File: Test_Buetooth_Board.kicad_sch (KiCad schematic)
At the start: 7 parts, among them U1 WH-BLE103a, U2 YM23, U3 HLK-B40, U4 WL6601-TC, U5 E104-BT52, U6 E104-BT01, U7 E104-BT5010A

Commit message: SCH: Se termina la primera versión del sch. PCB: Se ordenan unos componentes
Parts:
- added C1, C11, C13, C15, C16, C18, C19, C2, C21, C4, C5, C7, C9: 100n, 1-Capacitor:C_0805_2012Metric, symbol Device:C_Small
- added C10, C12, C14, C17, C20, C3, C8: 10n, 1-Capacitor:C_0805_2012Metric, symbol Device:C_Small
- added D1, D2, D3, D4, D5, D6, D7: LED, 1-Led:LED_0805, symbol Device:LED
- added J1: Screw_Terminal_01x04, Connector_PinHeader_2.54mm:PinHeader_1x04_P2.54mm_Vertical, symbol Connector:Screw_Terminal_01x04
- added J12, J13, J14, J15, J17, J18, J19, J20, J21, J22, J24, J25, J26, J29, J30, J31, J4, J5, J6, J7, J8, J9: Screw_Terminal_01x02, Connector_PinHeader_2.54mm:PinHeader_1x02_P2.54mm_Vertical, symbol Connector:Screw_Terminal_01x02
- added J16, J23, J27: Screw_Terminal_01x05, Connector_PinHeader_2.54mm:PinHeader_1x05_P2.54mm_Vertical, symbol Connector:Screw_Terminal_01x05
- added J28, J33: Screw_Terminal_01x06, Connector_PinHeader_2.54mm:PinHeader_1x06_P2.54mm_Vertical, symbol Connector:Screw_Terminal_01x06
- added J32: Screw_Terminal_01x07, 1-Pinhead:PinHeader_1x07_P2.54mm_Vertical, symbol Connector:Screw_Terminal_01x07
- added J34: Screw_Terminal_01x08, Connector_PinHeader_2.54mm:PinHeader_1x08_P2.54mm_Vertical, symbol Connector:Screw_Terminal_01x08
- added Q1, Q2, Q3, Q4, Q5, Q6, Q7: MMBT3904, Package_TO_SOT_SMD:SOT-23, symbol Transistor_BJT:MMBT3904
- added R1, R18, R2, R37, R41, R7: 100, 1-Resistor:R_0805_2012Metric, symbol Device:R_Small
- added R10, R13, R16, R17, R19, R21, R24, R26, R27, R29, R31, R32, R33, R35, R38, R39, R40, R42, R43, R5: 10k, 1-Resistor:R_0805_2012Metric, symbol Device:R_Small
- added R11, R15, R22, R25, R30, R36, R4: 2k2, 1-Resistor:R_0805_2012Metric, symbol Device:R_Small
- added R12, R20, R23, R28, R3, R34, R6, R9: 1k, 1-Resistor:R_0805_2012Metric, symbol Device:R_Small
- added R8: 10K, 1-Resistor:R_0805_2012Metric, symbol Device:R_Small
- added S1, S2, S3, S5, S6, S7, S8: 10-XX, 1-Switch:SW_PUSH_6mm_H7.3mm, symbol 1-Switch:10-XX
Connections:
- net GND: now reaches U3.1 (GND)
- net GND: now also U1.13 (GND), U1.15 (GND), U2.24 (GND), U3.10 (GND), U3.28 (GND), U4.2 (GND), U5.1 (GND), U5.12 (GND), U5.18 (GND), U5.5 (GND), U5.6 (GND), U6.1 (GND), U7.1 (GND), U7.16 (GND), U7.9 (GND), C1.2, C10.2, C11.2, C12.2, C13.2, C14.2, C15.2, C16.2, C17.2, C18.2, C19.2, C2.2, C20.2, C21.2, C3.2, C4.2, C5.2, C7.2, C8.2, C9.2, D3.1 (K), D4.1 (K), D5.1 (K), D7.1 (K), J1.4 (Pin_4), Q1.2 (E), Q2.2 (E), Q3.2 (E), Q4.2 (E), Q5.2 (E), Q6.2 (E), Q7.2 (E), R1.2, R10.2, R13.2, R16.2, R17.2, R18.2, R19.2, R2.2, R21.2, R24.2, R27.2, R29.2, R31.2, R32.2, R35.2, R37.2, R39.2, R40.2, R41.2, R5.2, R7.2
- net PC7_SLEEP_OUTPUT: now reaches U3.16 (PC7)
- net PC7_SLEEP_OUTPUT: now also J16.1 (Pin_1), R20.2
- net PC6_SLEEP_INPUT: now reaches U3.17 (PC6)
- net PC6_SLEEP_INPUT: now also J16.2 (Pin_2), R17.1
- net PC5_KEY_INPUT: now reaches U3.18 (PC5)
- net PC5_KEY_INPUT: now also J16.3 (Pin_3), R19.1
- net TX3: now reaches U3.23 (TXD)
- net TX3: now also J13.2 (Pin_2)
- net RX3: now reaches U3.24 (RXD)
- net RX3: now also J14.2 (Pin_2)
- net PA4_CONNECTED_OUTPUT: now reaches U3.25 (PA4)
- net PA4_CONNECTED_OUTPUT: now also J16.4 (Pin_4), R23.2
- net PA4_MODE_OUTPUT: now reaches U3.26 (PA5)
- net PA4_MODE_OUTPUT: now also J16.5 (Pin_5)
- net RST_3: now reaches U3.7 (RESET)
- net RST_3: now also R16.1, S5.3 (P)
- net VCC3: now reaches U3.9 (VBAT)
- net VCC3: now also C10.1, C9.1, J12.2 (Pin_2), R22.1, R25.1, S5.1 (S)
- net VCC7: now reaches U7.17 (VCC)
- net VCC7: now also C19.1, C20.1, J29.2 (Pin_2)
- net RX7: now reaches U7.18 (RXD)
- net RX7: now also J31.2 (Pin_2)
- net TX7: now reaches U7.19 (TXD)
- net TX7: now also J30.2 (Pin_2)
- net RTS_7: now reaches U7.20 (RTS)
- net RTS_7: now also J32.6 (Pin_6)
- net CTS_7: now reaches U7.21 (CTS)
- net CTS_7: now also J32.7 (Pin_7)
- net RST_7: now reaches U7.22 (RST)
- net RST_7: now also C21.1, R43.2, S8.1 (S)
- net MOD_7: now reaches U7.4 (MOD)
- net MOD_7: now also J32.1 (Pin_1), R39.1
- net WKP_7: now reaches U7.5 (WKP)
- net WKP_7: now also J32.2 (Pin_2), R40.1
- net DISC_7: now reaches U7.6 (DISC)
- net DISC_7: now also J32.3 (Pin_3), R42.2
- net LINK_7: now reaches U7.7 (LINK)
- net LINK_7: now also J32.4 (Pin_4)
- net DATA_7: now reaches U7.8 (DATA)
- net DATA_7: now also J32.5 (Pin_5)
- net SWCLK_5: now reaches U5.10 (CLK)
- net SWCLK_5: now also J23.2 (Pin_2)
- net WKP_5: now reaches U5.13 (WKP)
- net WKP_5: now also J23.3 (Pin_3), R27.1
- net TX5: now reaches U5.14 (TXD)
- net TX5: now also J20.2 (Pin_2)
- net RX5: now reaches U5.15 (RXD)
- net RX5: now also J21.2 (Pin_2)
- net LINK_5: now reaches U5.16 (LINK)
- net LINK_5: now also J23.4 (Pin_4), R28.2
- net DATA_5: now reaches U5.17 (DATA)
- net DATA_5: now also J23.5 (Pin_5)
- net VCC5: now reaches U5.3 (VCC)
- net VCC5: now also U5.4 (VH+), C13.1, C14.1, D6.2 (A), J22.2 (Pin_2), R26.1, R38.1, R43.1
- net RST_5: now reaches U5.7 (RST)
- net RST_5: now also C15.1, R26.2, S6.1 (S)
- net SWDIO_5: now reaches U5.8 (SWDIO)
- net SWDIO_5: now also J23.1 (Pin_1)
- net LINK_6: now reaches U6.10 (P1.5_LINK)
- net LINK_6: now also J27.4 (Pin_4), R34.2
- net DATA_6: now reaches U6.11 (P1.4_DATA)
- net DATA_6: now also J27.5 (Pin_5)
- net WKP_6: now reaches U6.13 (P1.2_WKP)
- net WKP_6: now also J28.1 (Pin_1), R32.1
- net P0.7: now reaches U6.16 (P0.7_AT)
- net P0.7: now also J28.2 (Pin_2)
- net P0.6: now reaches U6.17 (P0.6_AT)
- net P0.6: now also J28.3 (Pin_3)
- net DISC_6: now reaches U6.18 (P0.5_DISC)
- net DISC_6: now also J28.4 (Pin_4), R33.1
- net VCC6: now reaches U6.2 (VCC)
- net VCC6: now also C16.1, C17.1, J24.2 (Pin_2), R33.2, R36.1, R42.1
- net TX6: now reaches U6.20 (P0.3_TXD)
- net TX6: now also J25.2 (Pin_2)
- net RX6: now reaches U6.21 (P0.2_RXD)
- net RX6: now also J26.2 (Pin_2)
- net P0.1: now reaches U6.22 (P0.1_AT)
- net P0.1: now also J28.5 (Pin_5)
- net P0.0: now reaches U6.23 (P0.0_AT)
- net P0.0: now also J28.6 (Pin_6)
- net RST_6: now reaches U6.24 (RESET)
- net RST_6: now also C18.1, R38.2, S7.1 (S)
- net MODE_6: now reaches U6.5 (P2.0_MODE)
- net MODE_6: now also J27.1 (Pin_1), R31.1
- net SCL_6: now reaches U6.8 (SCL)
- net SCL_6: now also J27.2 (Pin_2)
- net SDA_6: now reaches U6.9 (SDA)
- net SDA_6: now also J27.3 (Pin_3)
- net VCC2: now reaches U2.1 (VCC)
- net VCC2: now also C7.1, C8.1, D1.2 (A), J7.2 (Pin_2), R15.1, R8.1
- net EINT2_2: now reaches U2.16 (EINT2)
- net EINT2_2: now also J33.4 (Pin_4)
- net ALED: now reaches U2.17 (ALED)
- net ALED: now also J33.5 (Pin_5), R12.2
- net TX2: now reaches U2.19 (TXD)
- net TX2: now also J8.2 (Pin_2)
- net RX2: now reaches U2.20 (RXD)
- net RX2: now also J9.2 (Pin_2)
- net EINT1_2: now reaches U2.21 (EINT1)
- net EINT1_2: now also J33.6 (Pin_6)
- net PWRC: now reaches U2.22 (PWRC)
- net PWRC: now also R8.2
- net RST_2: now reaches U2.23 (RST)
- net RST_2: now also C5.1, S3.1 (S)
- net OUTPUT1_2: now reaches U2.4 (OUTPUT1)
- net OUTPUT1_2: now also J33.1 (Pin_1)
- net OUTPUT2_2: now reaches U2.5 (OUTPUT2)
- net OUTPUT2_2: now also J33.2 (Pin_2)
- net STATUS: now reaches U2.6 (STATUS)
- net STATUS: now also J33.3 (Pin_3), R9.2
- net VCC4: now reaches U4.1 (VDD)
- net VCC4: now also C11.1, C12.1, J19.2 (Pin_2)
- net TX4: now reaches U4.3 (TX)
- net TX4: now also J17.2 (Pin_2)
- net RX4: now reaches U4.4 (RX)
- net RX4: now also J18.2 (Pin_2)
- net IO1: now reaches U4.5 (IO1)
- net IO1: now also J15.1 (Pin_1)
- net IO2: now reaches U4.6 (IO2)
- net IO2: now also J15.2 (Pin_2)
- net RELOAD_1: now reaches U1.1 (nReload)
- net RELOAD_1: now also C4.1, S1.1 (S)
- net RX1: now reaches U1.10 (UART_RX)
- net RX1: now also J6.2 (Pin_2)
- net LINK: now reaches U1.11 (LINK)
- net LINK: now also J34.7 (Pin_7), R3.2
- net RST_1: now reaches U1.12 (nRESET)
- net RST_1: now also C1.1, S2.1 (S)
- net VCC1: now reaches U1.14 (VBAT)
- net VCC1: now also U1.6 (VBAT), C2.1, C3.1, D2.2 (A), J4.2 (Pin_2)
- net GPIO3_1: now reaches U1.17 (GPIO3)
- net GPIO3_1: now also J34.8 (Pin_8)
- net WAKEUP_1: now reaches U1.2 (Wake)
- net WAKEUP_1: now also J34.1 (Pin_1)
- net at U1.3 (GPIO1): now also R6.1
- net ADC_1: now reaches U1.4 (ADC)
- net ADC_1: now also J34.3 (Pin_3)
- net GPIO2_1: now reaches U1.5 (GPIO2)
- net GPIO2_1: now also J34.4 (Pin_4)
- net SWCLK_1: now reaches U1.7 (SWCLK)
- net SWCLK_1: now also J34.5 (Pin_5)
- net SWDIO_1: now reaches U1.8 (SWDIO)
- net SWDIO_1: now also J34.6 (Pin_6)
- net TX1: now reaches U1.9 (UART_TX)
- net TX1: now also J5.2 (Pin_2)
- new net: D3.2 (A), Q4.3 (C), R22.2
- new net: Q3.1 (B), R12.1, R13.1
- new net: Q7.1 (B), R34.1, R35.1
- new net: D5.2 (A), Q5.3 (C), R25.2
- new net: R2.1, S2.3 (P)
- new net: D4.2 (A), Q3.3 (C), R15.2
- new net: Q5.1 (B), R23.1, R24.1
- new net: D2.1 (K), R4.1
- new net: R7.1, S3.3 (P)
- new net: R41.1, S8.3 (P)
- new net: Q2.1 (B), R10.1, R9.1
- new net: R37.1, S7.3 (P)
- new net: Q1.3 (C), R4.2
- new net: D7.2 (A), Q7.3 (C), R36.2
- new net: Q4.1 (B), R20.1, R21.1
- new net: Q1.1 (B), R3.1, R5.1
- new net: Q6.1 (B), R28.1, R29.1
- new net: D1.1 (K), R11.1
- new net: Q2.3 (C), R11.2
- new net: R18.1, S6.3 (P)
- new net: Q6.3 (C), R30.2
- new net: D6.1 (K), R30.1
- new net: R1.1, S1.3 (P)
- new net +3.3V: J1.1 (Pin_1), J12.1 (Pin_1), J19.1 (Pin_1), J22.1 (Pin_1), J24.1 (Pin_1), J29.1 (Pin_1), J4.1 (Pin_1), J7.1 (Pin_1)
- new net GPIO1_1: J34.2 (Pin_2), R6.2
- new net RX: J1.3 (Pin_3), J14.1 (Pin_1), J18.1 (Pin_1), J21.1 (Pin_1), J26.1 (Pin_1), J31.1 (Pin_1), J6.1 (Pin_1), J9.1 (Pin_1)
- new net TX: J1.2 (Pin_2), J13.1 (Pin_1), J17.1 (Pin_1), J20.1 (Pin_1), J25.1 (Pin_1), J30.1 (Pin_1), J5.1 (Pin_1), J8.1 (Pin_1)
- no-connect marks 0 -> 3
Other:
- note added: "IO1,IO2: None"
- note added: "MOD: Mode selection input pin. Low: Configuration Mode, High: Transparent Mode WKP: Wake up input pin. FallingEdge: WakeUp, RisingEdge: Sleep. DISC: Disconnection, internall pull-up. FallingEdge: Disconnect LINK: Output data indicator. It's not clear DATA: Data indicator RTS CTS RST: Reset pin. Low: Reset, High: No reset"
- note added: "ON: Connected"
- note added: "ON: Linked"
- note added: "ON: Sleep"
- note added: "P2.0_MOD: Mode setting. FallingEdge: Configuration Mode, RisingEdge: Transparent Mode P1.5_LINK: Status output pin. Low: Connected, High: Disconnected P1.4_DATA: It's used to do data framing. P1.2_WAKEUP: FallingEdge:WakeUp, RisingEdge:Sleep P0.7: Output pin P0.6: Output pin P0.5: Disconnecting input pin. FallingEdge: Disconnect current connection. P0.3: TX P0.2: RX P0.1: Input pin P0.0: Input pi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"
- note added: "RESET restarts module: High: Reset VCHG used only with battery. VBAT: 3.3V PC7: Sleep state indicator. High: Full Speed PC6: Hibernation: High: Go Hibernation, Low: Exit Hibernation PC5: Blocking input: Low: Module ON, High: Module OFF PA4: Bluetooth connection status output. Low: Connected, High: Disconnected PA5: Mode output indicator. High: Master, Low: Slave"
- note added: "STATUS indicates if BL is broadcasting: ON: BL is working, OFF: BL isn't working. ALED indicates if bluetooth is on. Low: BL ON, High: BL OFF. PWRC is used to wake up BL. High: Wake Up, Low: Sleep when BL is connected RESET resets BL and it has an internall pul-up. Active: Low"
- note added: "VH+ connected to VCC RST: Reset pin. Low: Reset, High: No reset SWDIO: JTAG interface SWCLK: JTAG interface WKP: WakeUp input pin: FallingEdge: WakeUp. RisingEdge: Sleep LINK: output status. High: Linked. Low: No linked DATA: It's used to do data framing."
- note added: "nReload has a 10k internall pull-up. Active:Low nReset has a 100k internall pull-up. Active: Low WakeUp has an internall up. Active:Low GPIO1 is a control pin to download firmware by serial port (besides SWCLK & SWDIO) GPIO1, GPIO2, GPIO3 and ADC pins are reserved and the funcionality of them depends of manufacter."
- moved on the sheet: U2, U3, U4, U5, U6, U7

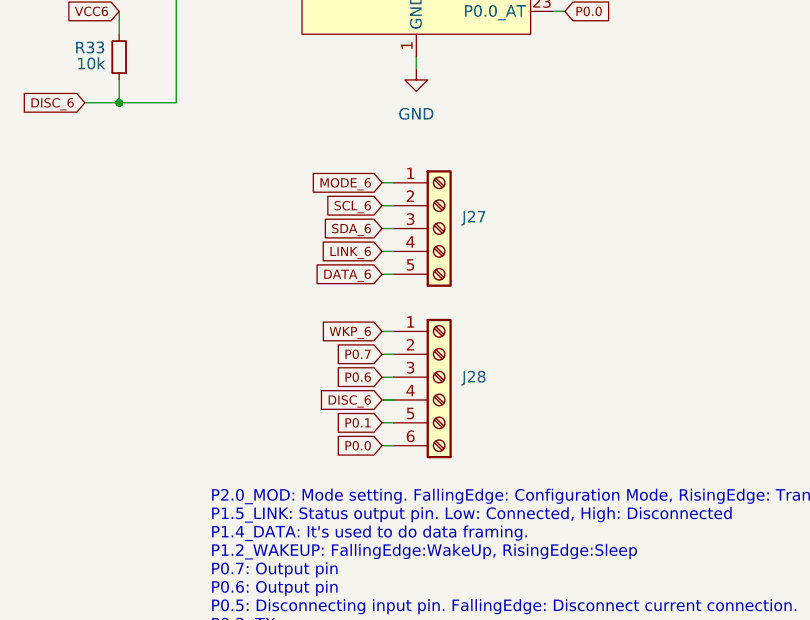
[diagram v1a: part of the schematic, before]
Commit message: Se añade descripción a la cajetilla y se unen dos headers en uno
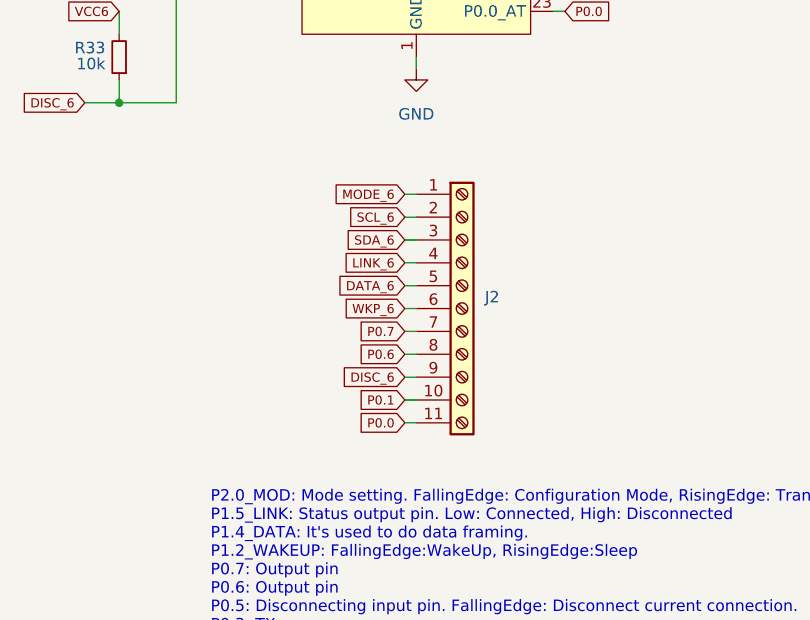
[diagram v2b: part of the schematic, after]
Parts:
- removed J27: Screw_Terminal_01x05, Connector_PinHeader_2.54mm:PinHeader_1x05_P2.54mm_Vertical, symbol Connector:Screw_Terminal_01x05
- removed J28: Screw_Terminal_01x06, Connector_PinHeader_2.54mm:PinHeader_1x06_P2.54mm_Vertical, symbol Connector:Screw_Terminal_01x06
- added J2: Screw_Terminal_01x11, Connector_PinHeader_2.54mm:PinHeader_1x11_P2.54mm_Vertical, symbol Connector:Screw_Terminal_01x11
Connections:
- net DATA_6: now also J2.5 (Pin_5)
- net DISC_6: now also J2.9 (Pin_9)
- net LINK_6: now also J2.4 (Pin_4)
- net MODE_6: now also J2.1 (Pin_1)
- net P0.0: now also J2.11 (Pin_11)
- net P0.1: now also J2.10 (Pin_10)
- net P0.6: now also J2.8 (Pin_8)
- net P0.7: now also J2.7 (Pin_7)
- net SCL_6: now also J2.2 (Pin_2)
- net SDA_6: now also J2.3 (Pin_3)
- net WKP_6: now also J2.6 (Pin_6)
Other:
- company: (none) -> Eplimin
- title: (none) -> Placa para pruebas con módulos Bluetooth

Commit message: Se acaba de colocar un header por cada placa para probar en otra próxima rama la utilidad, en main seguiremos con el planteamiento inicial de utiizar jumpers
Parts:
- added J10: Screw_Terminal_01x09, Connector_PinHeader_2.54mm:PinHeader_1x09_P2.54mm_Vertical, symbol Connector:Screw_Terminal_01x09
- added J11, J28: Screw_Terminal_01x08, Connector_PinHeader_2.54mm:PinHeader_1x08_P2.54mm_Vertical, symbol Connector:Screw_Terminal_01x08
- added J27: Screw_Terminal_01x05, Connector_PinHeader_2.54mm:PinHeader_1x05_P2.54mm_Vertical, symbol Connector:Screw_Terminal_01x05
- added J3: Screw_Terminal_01x11, Connector_PinHeader_2.54mm:PinHeader_1x11_P2.54mm_Vertical, symbol Connector:Screw_Terminal_01x11
- added J35: Screw_Terminal_01x14, symbol Connector:Screw_Terminal_01x14
- added J36: Screw_Terminal_01x10, symbol Connector:Screw_Terminal_01x10
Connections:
- net ADC_1: now also J3.4 (Pin_4)
- net ALED: now also J10.6 (Pin_6)
- net CTS_7: now also J36.10 (Pin_10)
- net DATA_5: now also J28.8 (Pin_8)
- net DATA_6: now also J35.6 (Pin_6)
- net DATA_7: now also J36.5 (Pin_5)
- net DISC_6: now also J35.10 (Pin_10)
- net DISC_7: now also J36.3 (Pin_3)
- net EINT1_2: now also J10.9 (Pin_9)
- net EINT2_2: now also J10.5 (Pin_5)
- net GPIO1_1: now also J3.2 (Pin_2)
- net GPIO2_1: now also J3.5 (Pin_5)
- net GPIO3_1: now also J3.11 (Pin_11)
- net IO1: now also J27.4 (Pin_4)
- net IO2: now also J27.5 (Pin_5)
- net LINK: now also J3.10 (Pin_10)
- net LINK_5: now also J28.7 (Pin_7)
- net LINK_6: now also J35.5 (Pin_5)
- net LINK_7: now also J36.4 (Pin_4)
- net MODE_6: now also J35.2 (Pin_2)
- net MOD_7: now also J36.1 (Pin_1)
- net OUTPUT1_2: now also J10.2 (Pin_2)
- net OUTPUT2_2: now also J10.3 (Pin_3)
- net P0.0: now also J35.14 (Pin_14)
- net P0.1: now also J35.13 (Pin_13)
- net P0.6: now also J35.9 (Pin_9)
- net P0.7: now also J35.8 (Pin_8)
- net PA4_CONNECTED_OUTPUT: now also J11.7 (Pin_7)
- net PA4_MODE_OUTPUT: now also J11.8 (Pin_8)
- net PC5_KEY_INPUT: now also J11.4 (Pin_4)
- net PC6_SLEEP_INPUT: now also J11.3 (Pin_3)
- net PC7_SLEEP_OUTPUT: now also J11.2 (Pin_2)
- net RTS_7: now also J36.9 (Pin_9)
- net RX1: now also J3.9 (Pin_9)
- net RX2: now also J10.8 (Pin_8)
- net RX3: now also J11.6 (Pin_6)
- net RX4: now also J27.3 (Pin_3)
- net RX5: now also J28.6 (Pin_6)
- net RX6: now also J35.12 (Pin_12)
- net RX7: now also J36.7 (Pin_7)
- net SCL_6: now also J35.3 (Pin_3)
- net SDA_6: now also J35.4 (Pin_4)
- net STATUS: now also J10.4 (Pin_4)
- net SWCLK_1: now also J3.6 (Pin_6)
- net SWCLK_5: now also J28.3 (Pin_3)
- net SWDIO_1: now also J3.7 (Pin_7)
- net SWDIO_5: now also J28.2 (Pin_2)
- net TX1: now also J3.8 (Pin_8)
- net TX2: now also J10.7 (Pin_7)
- net TX3: now also J11.5 (Pin_5)
- net TX4: now also J27.2 (Pin_2)
- net TX5: now also J28.5 (Pin_5)
- net TX6: now also J35.11 (Pin_11)
- net TX7: now also J36.8 (Pin_8)
- net VCC1: now also J3.3 (Pin_3)
- net VCC2: now also J10.1 (Pin_1)
- net VCC3: now also J11.1 (Pin_1)
- net VCC4: now also J27.1 (Pin_1)
- net VCC5: now also J28.1 (Pin_1)
- net VCC6: now also J35.1 (Pin_1)
- net WAKEUP_1: now also J3.1 (Pin_1)
- net WKP_5: now also J28.4 (Pin_4)
- net WKP_6: now also J35.7 (Pin_7)
- net WKP_7: now also J36.2 (Pin_2)
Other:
- moved on the sheet: C10, C9, J12, J13, J14, J16, J23

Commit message: SCH: Se modificaron VCC que no estaban en el orden correcto, re remplaza la librería del pulsador, se areglan otros errores, tener en cuenta para la otra rama o eliminarla. PCB: Ruteado, falta terminar GND y revisar conexiones
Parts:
- removed J10: Screw_Terminal_01x09, Connector_PinHeader_2.54mm:PinHeader_1x09_P2.54mm_Vertical, symbol Connector:Screw_Terminal_01x09
- removed J11, J28: Screw_Terminal_01x08, Connector_PinHeader_2.54mm:PinHeader_1x08_P2.54mm_Vertical, symbol Connector:Screw_Terminal_01x08
- removed J27: Screw_Terminal_01x05, Connector_PinHeader_2.54mm:PinHeader_1x05_P2.54mm_Vertical, symbol Connector:Screw_Terminal_01x05
- removed J3: Screw_Terminal_01x11, Connector_PinHeader_2.54mm:PinHeader_1x11_P2.54mm_Vertical, symbol Connector:Screw_Terminal_01x11
- removed J35: Screw_Terminal_01x14, symbol Connector:Screw_Terminal_01x14
- removed J36: Screw_Terminal_01x10, symbol Connector:Screw_Terminal_01x10
- removed R6: 1k, 1-Resistor:R_0805_2012Metric, symbol Device:R_Small
- removed S1, S2, S3, S5, S6, S7, S8: 10-XX, 1-Switch:SW_PUSH_6mm_H7.3mm, symbol 1-Switch:10-XX
- added S1, S2, S3, S4, S5, S6, S7: SW_PUSH_6mm_H7.3mm, 1-Switch:SW_PUSH_6mm_H7.3mm, symbol 1-Switch:SW_PUSH_6mm_H7.3mm
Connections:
- net GPIO1_1: now also U1.3 (GPIO1)
- net RELOAD_1: now also S1.2, S1.4
- net RST_1: now also S4.2, S4.4
- net RST_2: now also S2.2, S2.4
- net RST_3: now also S3.1, S3.3
- net RST_5: now also S5.2, S5.4
- net RST_6: now also S6.2, S6.4
- net RST_7: now also S7.2, S7.4
- net VCC3: now also S3.2, S3.4
- net VCC5: no longer R38.1, R43.1
- net VCC6: now also R38.1; no longer R42.1
- net VCC7: now also R42.1, R43.1
- net at R2.1: now also S4.1, S4.3
- net at R7.1: now also S2.1, S2.3
- net at R41.1: now also S7.1, S7.3
- net at R37.1: now also S6.1, S6.3
- net at R18.1: now also S5.1, S5.3
- net at R1.1: now also S1.1, S1.3
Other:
- moved on the sheet: C18, C21, J23, R38, R41, R43

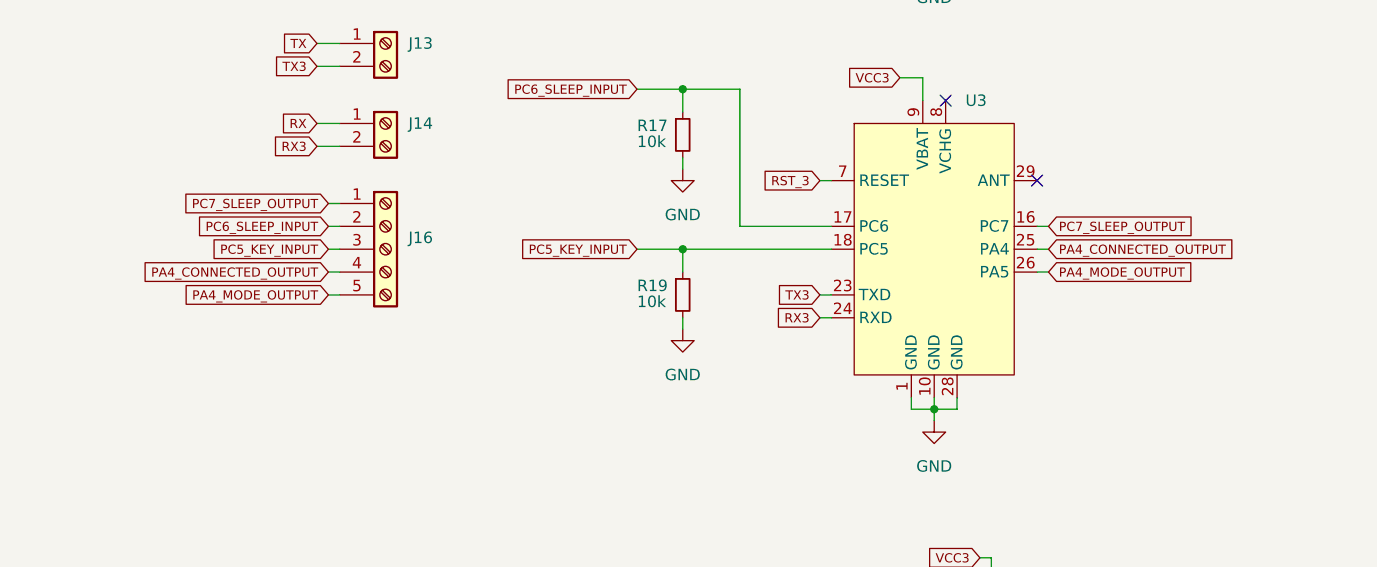
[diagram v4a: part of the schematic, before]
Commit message: SCH: Se corrige una etiqueta. PCB: Se añaden y ordenan las referencias. JLC: No hay cambios
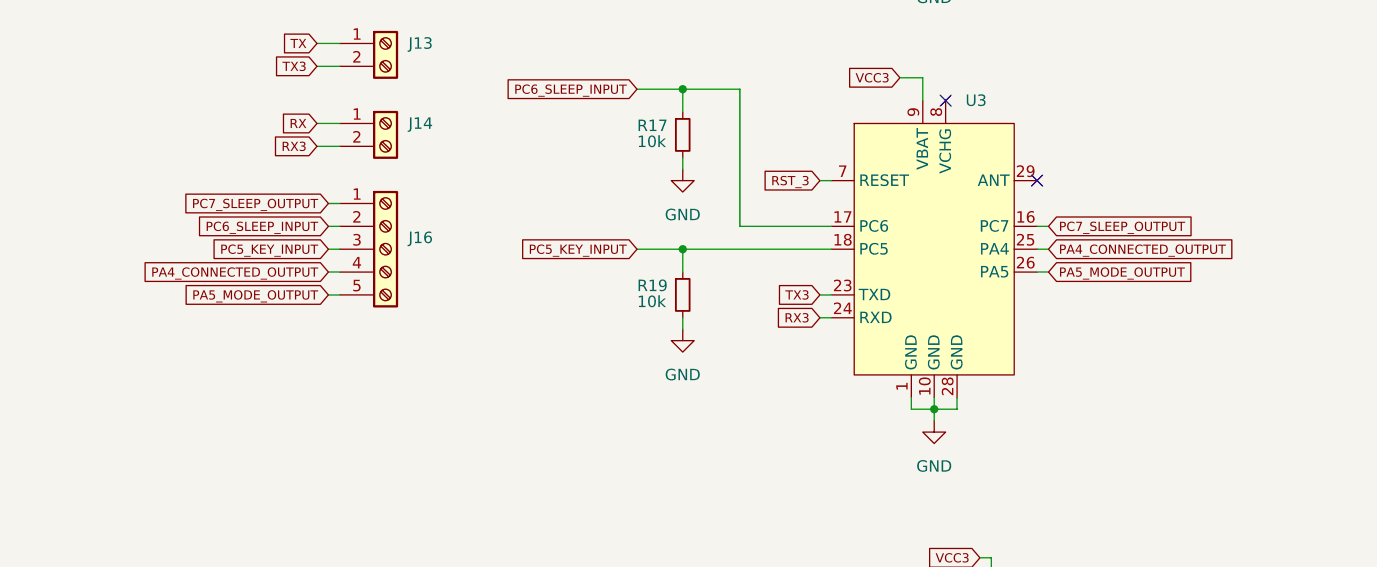
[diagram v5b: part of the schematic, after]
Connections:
- net PA4_MODE_OUTPUT renamed PA5_MODE_OUTPUT
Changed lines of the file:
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@@
 		)
 	)
-	(global_label "PA4_MODE_OUTPUT"
+	(global_label "PA5_MODE_OUTPUT"
 		(shape input)
 		(at 372.11 99.06 0)
@@
 		)
 	)
-	(global_label "PA4_MODE_OUTPUT"
+	(global_label "PA5_MODE_OUTPUT"
 		(shape input)
 		(at 292.1 101.6 180)

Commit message: SCH: Se agregan leds para el VCC de cada módulo, se cambia la librería del pulsador. se mueven posiciones. PCB: Se agrega serigrafía, se agregan vías gnd, se modifica GND, se resuelven los errores. JLCPCB: Se agrega el #part, se actualiza el archivo.
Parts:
- added D10, D11, D12, D13, D14, D8, D9: GREEN, 1-Led:LED_0805, symbol Device:LED
- added R14, R44, R45, R46, R47, R48, R6: 1k, 1-Resistor:R_0805_2012Metric, symbol Device:R_Small
- D1, D2, D3, D4, D5, D6, D7: value LED -> RED
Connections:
- net GND: now also R14.2, R44.2, R45.2, R46.2, R47.2, R48.2, R6.2
- net RELOAD_1: now also S1.3; no longer S1.2, S1.4
- net RST_1: no longer S4.2
- net RST_2: now also S2.3; no longer S2.2, S2.4
- net RST_3: no longer S3.3
- net RST_5: no longer S5.2
- net RST_6: no longer S6.2
- net RST_7: no longer S7.2
- net VCC1: now also D8.2 (A)
- net VCC2: now also D9.2 (A)
- net VCC3: now also D10.2 (A); no longer S3.2
- net VCC4: now also D11.2 (A)
- net VCC5: now also D12.2 (A)
- net VCC6: now also D14.2 (A)
- net VCC7: now also D13.2 (A)
- net at R37.1, S6.1: no longer S6.3
- net at R18.1, S5.1: no longer S5.3
- net at R7.1, S2.1: no longer S2.3
- net at R1.1, S1.1: no longer S1.3
- new net: D8.1 (K), R6.1
- new net: D11.1 (K), R45.1
- new net: D13.1 (K), R47.1
- new net: D14.1 (K), R48.1
- new net: D9.1 (K), R14.1
- new net: R2.1, S4.2
- new net: D12.1 (K), R46.1
- new net: R41.1, S7.2
- new net: D10.1 (K), R44.1
- now unconnected: S4.1, S4.3, S7.1, S7.3
- no-connect marks 3 -> 17
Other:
- moved on the sheet: C16, C17, J1, J24, J25, J26
